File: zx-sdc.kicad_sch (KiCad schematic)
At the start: 65 parts, among them J1 SD_Card, J2 Micro_SD_Card_Det2, J3 Conn_01x02_Pin, Q1 2N7000, Q2 BC557, U1 74LS688, U10 74LS125, U11 74LS595, U12 74LS30, U13 74LS138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

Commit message: preparation for board design
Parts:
- C5, C6, C9: value C -> 0.1u
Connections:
- net +5V: now also U12.1, U12.14 (VCC); no longer U12.12, U2.16 (VCC)
- net A0: now also U12.2; no longer U12.1
- net A1: now also U12.3; no longer U12.2
- net A2: now also U12.4; no longer U12.3
- net A4: now also U12.5; no longer U12.4
- net A6: now also U12.6; no longer U12.5
- net GND: now also U12.7 (GND); no longer U2.8 (GND)
- net at U12.11: now also U6.10; no longer U6.12
- new net: U12.12, U6.12
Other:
- moved on the sheet: U1, U12A, U12B, U13, U2A, U2B, U6E, U6F

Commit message: completed design of ZX SDC
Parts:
- removed J3: Conn_01x02_Pin, symbol Connector:Conn_01x02_Pin
- removed R11: 4k7, symbol Device:R
- added C11: 0.1u, Capacitor_THT:C_Disc_D4.7mm_W2.5mm_P5.00mm, symbol Device:C
- added J4: Conn_01x03_Pin, Connector_PinHeader_2.54mm:PinHeader_1x03_P2.54mm_Vertical, symbol Connector:Conn_01x03_Pin
- C1, C2, C5, C6, C9: footprint (none) -> Capacitor_THT:C_Disc_D4.7mm_W2.5mm_P5.00mm
- C10, C3, C4: footprint (none) -> Capacitor_THT:CP_Radial_D5.0mm_P2.00mm
- C7, C8: value C -> 0.1u; footprint (none) -> Capacitor_THT:C_Disc_D4.7mm_W2.5mm_P5.00mm
- D11, D8: footprint (none) -> LED_THT:LED_D3.0mm
- J1: footprint (none) -> Connector_Card:SD_TE_2041021
- J2: footprint (none) -> Connector_Card:microSD_HC_Hirose_DM3AT-SF-PEJM5
- Q1, Q2: footprint Package_TO_SOT_THT:TO-92_Inline -> Package_TO_SOT_THT:TO-92_Inline_Wide
- R1, R10, R12, R13, R14, R15, R16, R17, R18, R19, R2, R20, R21, R22, R23, R24, R3, R4, R5, R6, R7, R8, R9: footprint (none) -> Resistor_THT:R_Axial_DIN0204_L3.6mm_D1.6mm_P5.08mm_Horizontal
- U10, U12, U6, U9: footprint (none) -> Package_DIP:DIP-14_W7.62mm
- U11, U13, U4, U5, U7: footprint (none) -> Package_DIP:DIP-16_W7.62mm
- U8: footprint Connector_Card:SD_Hirose_DM1AA_SF_PEJ82 -> Package_DIP:DIP-14_W7.62mm
- Y1: footprint (none) -> Crystal:Crystal_HC18-U_Vertical
- Z1: footprint (none) -> RobikBUS:ZXBUS Slot Connector
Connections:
- net +3.3V: no longer R23.1
- net +5V: now also R23.1, U8.10 (~{S}), C11.1
- net GND: now also C11.2
- net SPI_MISO: now also J4.2 (Pin_2); no longer U5.14 (SER)
- net at U8.9 (Q): now also J4.3 (Pin_3)
- net at D11.1 (K): now also U9.6 (~{Q}); no longer U9.5 (Q)
- new net: J4.1 (Pin_1), U5.14 (SER)
- no-connect marks 52 -> 53
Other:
- moved on the sheet: D11, R23

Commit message: refinings & last cuts
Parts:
- removed U1: 74LS688, symbol 74xx:74LS688
- removed U2: 74LS139, symbol 74xx:74LS139
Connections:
- no-connect marks 53 -> 49
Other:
- added sheet Alternative port decoder (alt-port-decoder.kicad_sch)

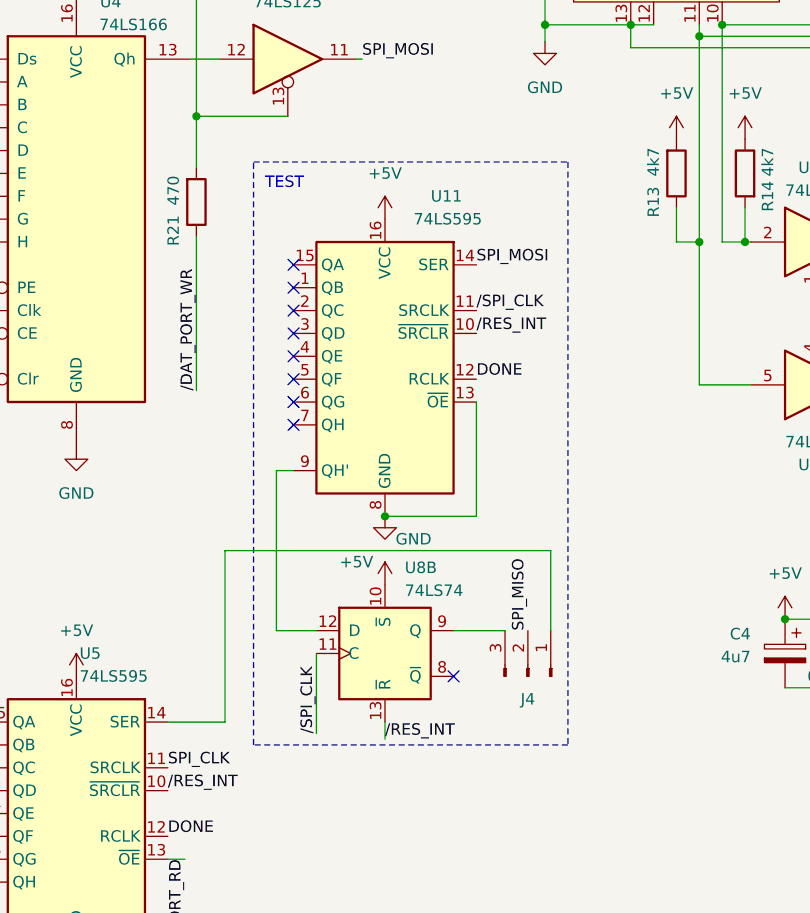
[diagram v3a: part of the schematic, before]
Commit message: fixed and annotated SD/TEST jumpers
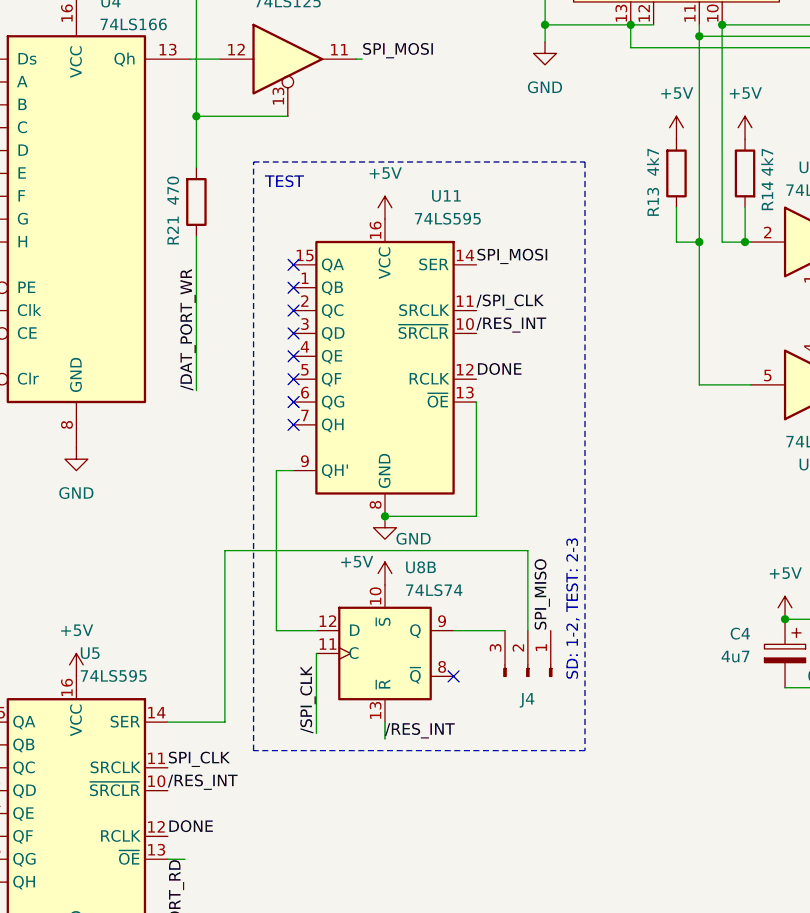
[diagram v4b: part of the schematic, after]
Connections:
- net SPI_MISO: now also J4.1 (Pin_1); no longer J4.2 (Pin_2)
- net at U5.14 (SER): now also J4.2 (Pin_2); no longer J4.1 (Pin_1)
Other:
- note added: "SD: 1-2, TEST: 2-3"
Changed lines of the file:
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@@
-    (stroke (width 0) (type default))
-  )
-  (wire (pts (xy 208.915 142.875) (xy 208.915 151.765))
     (stroke (width 0) (type default))
   )
@@
     (stroke (width 0) (type default))
   )
-  (wire (pts (xy 172.72 142.875) (xy 208.915 142.875))
+  (wire (pts (xy 172.72 142.875) (xy 206.375 142.875))
     (stroke (width 0) (type default))
   )
@@
     (stroke (width 0) (type default))
   )
+  (wire (pts (xy 206.375 142.875) (xy 206.375 151.765))
+    (stroke (width 0) (type default))
+  )
   (wire (pts (xy 196.215 66.04) (xy 207.01 66.04))
     (stroke (width 0) (type default))
@@
     (stroke (width 0) (type default))
   )
-  (rectangle (start 175.895 99.695) (end 210.82 164.465)
+  (rectangle (start 175.895 99.695) (end 212.725 165.1)
     (stroke (width 0) (type dash))
     (fill (type none))
   )
+  (text "SD: 1-2, TEST: 2-3" (at 212.09 157.48 90)
+    (effects (font (size 1.27 1.27)) (justify left bottom))
+  )
   (text "TEST" (at 177.165 102.87 0)
     (effects (font (size 1.27 1.27)) (justify left bottom))
@@
     (effects (font (size 1.27 1.27)) (justify left bottom))
   )
+  (label "SPI_MISO" (at 208.915 151.765 90) (fields_autoplaced)
+    (effects (font (size 1.27 1.27)) (justify left bottom))
+  )
   (label "D7" (at 146.05 179.705 180) (fields_autoplaced)
     (effects (font (size 1.27 1.27)) (justify right bottom))
@@
     (effects (font (size 1.27 1.27)) (justify left bottom))
   )
-  (label "SPI_MISO" (at 206.375 151.765 90) (fields_autoplaced)
-    (effects (font (size 1.27 1.27)) (justify left bottom))
-  )
